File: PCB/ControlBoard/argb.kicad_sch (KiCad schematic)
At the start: 6 parts, among them J3 ARGB, U3 74AHC2G125

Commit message: First pass of PCB rework.
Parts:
- C6: footprint Capacitor_SMD:C_0805_2012Metric -> Capacitor_SMD:C_0603_1608Metric
- R3: footprint Resistor_SMD:R_0805_2012Metric -> Resistor_SMD:R_0603_1608Metric
- U3: footprint (none) -> Package_SO:TSSOP-8_3x3mm_P0.65mm
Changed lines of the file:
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@@
       (effects (font (size 1.27 1.27)) (justify left) hide)
     )
-    (property "Footprint" "" (at 33.02 22.86 0)
+    (property "Footprint" "Package_SO:TSSOP-8_3x3mm_P0.65mm" (at 33.02 22.86 0)
       (effects (font (size 1.27 1.27)) hide)
     )
@@
       (effects (font (size 1.27 1.27)))
     )
-    (property "Footprint" "" (at 68.58 24.13 0)
+    (property "Footprint" "Package_SO:TSSOP-8_3x3mm_P0.65mm" (at 68.58 24.13 0)
       (effects (font (size 1.27 1.27)) hide)
     )
@@
       (effects (font (size 1.27 1.27)))
     )
-    (property "Footprint" "" (at 68.58 39.37 0)
+    (property "Footprint" "Package_SO:TSSOP-8_3x3mm_P0.65mm" (at 68.58 39.37 0)
       (effects (font (size 1.27 1.27)) hide)
     )
@@
       (effects (font (size 1.27 1.27)) (justify left))
     )
-    (property "Footprint" "Capacitor_SMD:C_0805_2012Metric" (at 20.32 29.21 0)
+    (property "Footprint" "Capacitor_SMD:C_0603_1608Metric" (at 20.32 29.21 0)
       (effects (font (size 1.27 1.27)) hide)
     )
@@
       (effects (font (size 1.27 1.27)) (justify left))
     )
-    (property "Footprint" "Resistor_SMD:R_0805_2012Metric" (at 35.56 54.61 0)
+    (property "Footprint" "Resistor_SMD:R_0603_1608Metric" (at 35.56 54.61 0)
       (effects (font (size 1.27 1.27)) hide)
     )
@@
       (effects (font (size 1.27 1.27)) (justify left))
     )
-    (property "Footprint" "Resistor_SMD:R_0805_2012Metric" (at 35.56 62.23 0)
-      (effects (font (size 1.27 1.27)) hide)
-    )
+    (property "Footprint" "Resistor_SMD:R_0603_1608Metric" (at 35.56 62.23 0)
+      (effects (font (size 1.27 1.27)) hide)
+    )

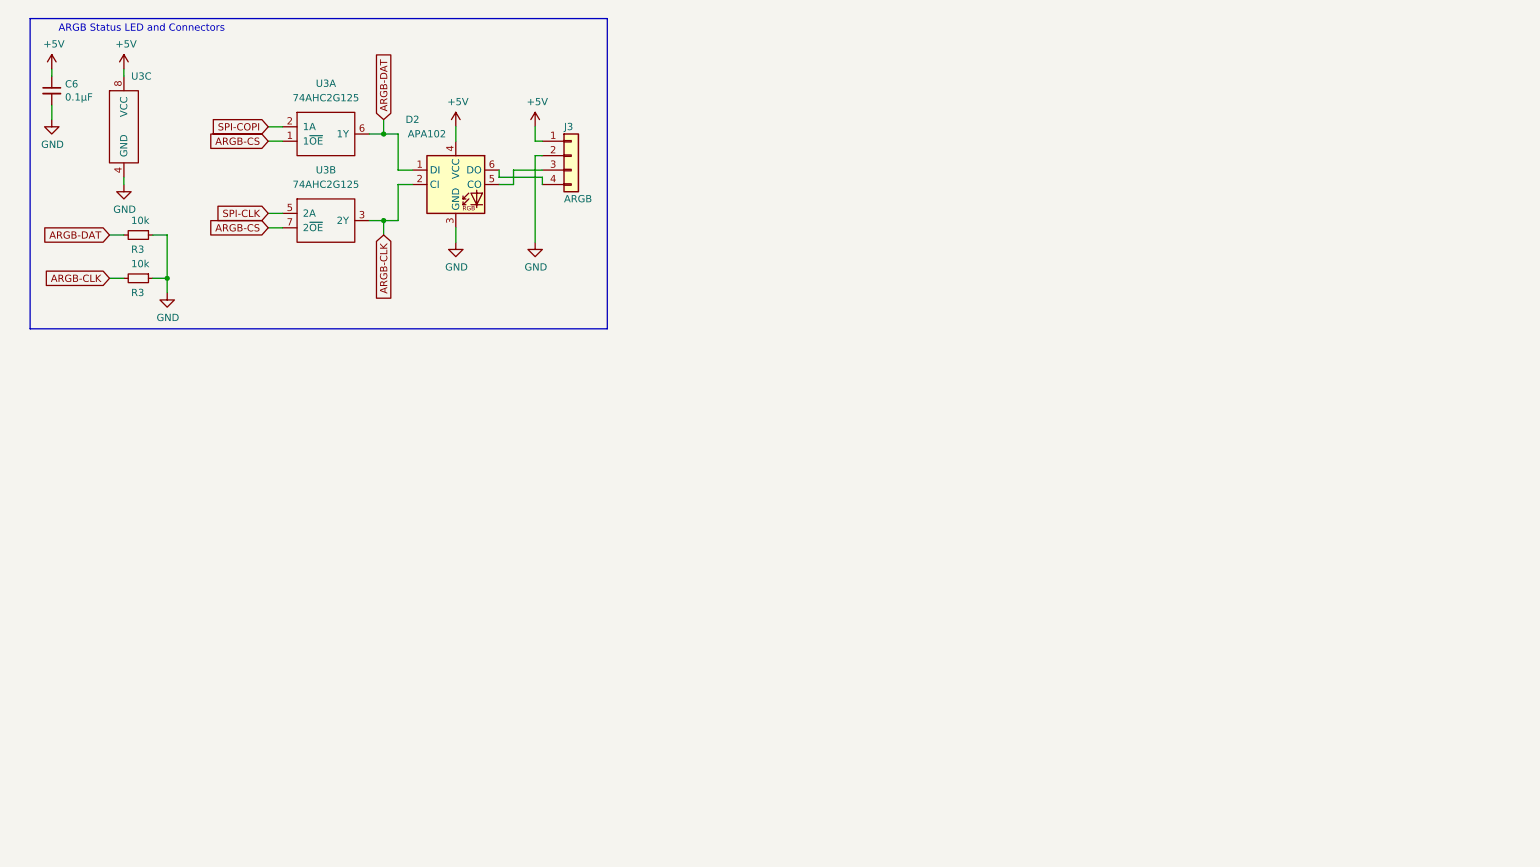
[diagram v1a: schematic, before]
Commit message: ControlBoard B02, with buck regulator fix.
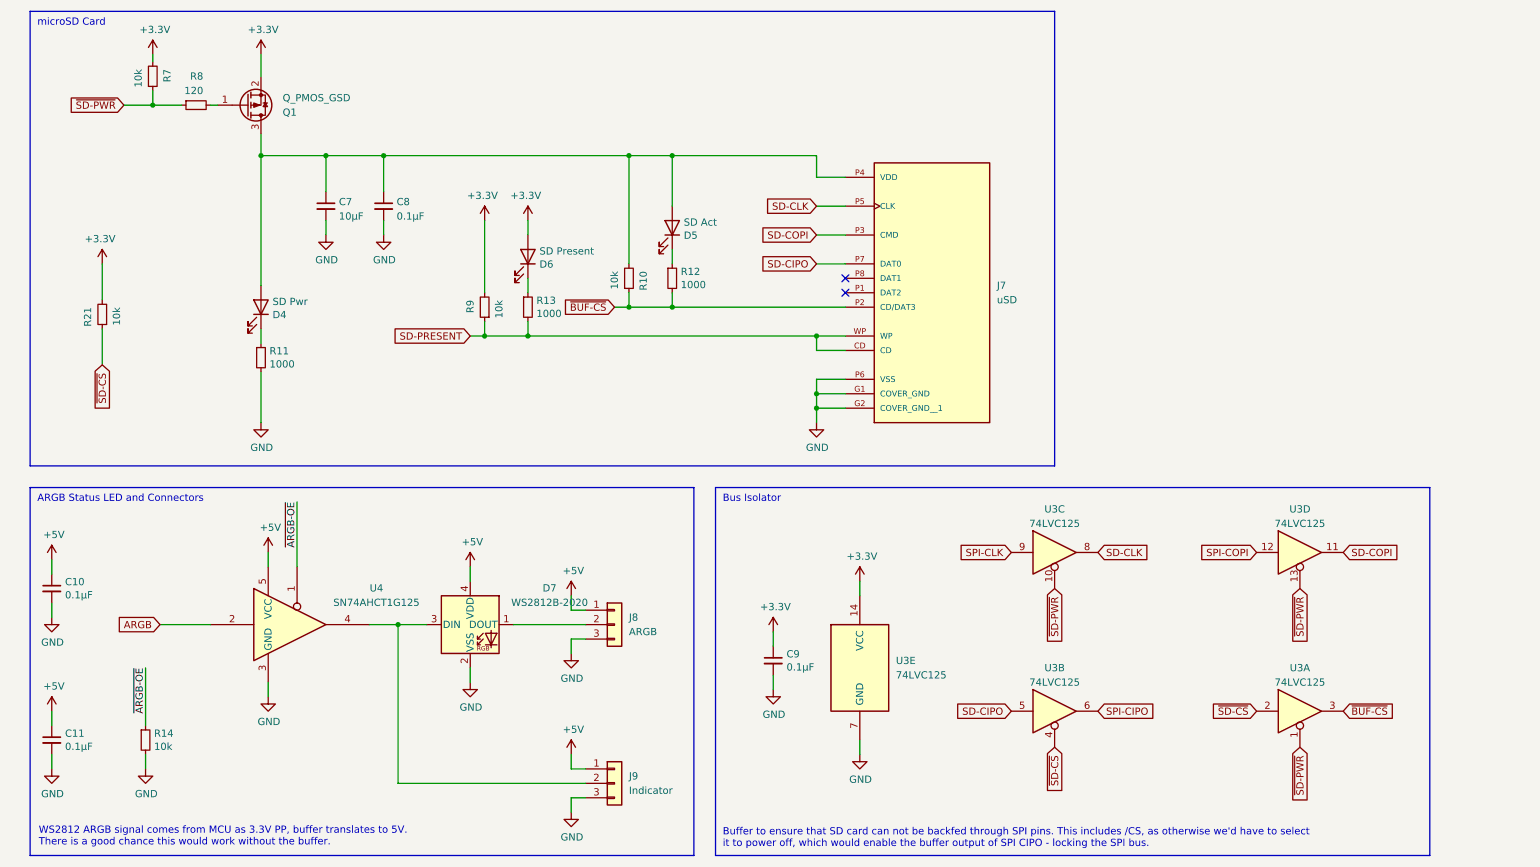
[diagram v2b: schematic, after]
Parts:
- removed C6: 0.1μF, Capacitor_SMD:C_0603_1608Metric, symbol Device:C_Small
- removed D2: APA102, LED_SMD:LED_RGB_5050-6, symbol LED:APA102
- removed J3: ARGB, Connector_JST:JST_PH_B4B-PH-SM4-TB_1x04-1MP_P2.00mm_Vertical, symbol Connector_Generic:Conn_01x04
- removed R3 (x2): 10k, Resistor_SMD:R_0603_1608Metric, symbol Device:R_Small
- removed U3: 74AHC2G125, Package_SO:TSSOP-8_3x3mm_P0.65mm, symbol KTANE:74AHC2G125
- added C10, C11, C8, C9: 0.1μF, Capacitor_SMD:C_0603_1608Metric, symbol Device:C_Small
- added C7: 10μF, Capacitor_SMD:C_0603_1608Metric, symbol Device:C_Small
- added D4: SD Pwr, LED_SMD:LED_0603_1608Metric, symbol Device:LED
- added D5: SD Act, LED_SMD:LED_0603_1608Metric, symbol Device:LED
- added D6: SD Present, LED_SMD:LED_0603_1608Metric, symbol Device:LED
- added D7: WS2812B-2020, LED_SMD:LED_WS2812B-2020_PLCC4_2.0x2.0mm, symbol LED:WS2812B-2020
- added J7: uSD, KTANE:CUI_MSD-11-A, symbol KTANE:MSD-11-A
- added J8: ARGB, Connector_JST:JST_PH_B3B-PH-SM4-TB_1x03-1MP_P2.00mm_Vertical, symbol Connector_Generic:Conn_01x03
- added J9: Indicator, Connector_JST:JST_PH_B3B-PH-SM4-TB_1x03-1MP_P2.00mm_Vertical, symbol Connector_Generic:Conn_01x03
- added Q1: Q_PMOS_GSD, Package_TO_SOT_SMD:SOT-23, symbol Transistor_FET:Q_PMOS_GSD
- added R10, R14, R21, R7, R9: 10k, Resistor_SMD:R_0603_1608Metric, symbol Device:R_Small
- added R11, R12, R13: 1000, Resistor_SMD:R_0603_1608Metric, symbol Device:R_Small
- added R8: 120, Resistor_SMD:R_0603_1608Metric, symbol Device:R_Small
- added U3: 74LVC125, Package_SO:TSSOP-14_4.4x5mm_P0.65mm, symbol 74xx:74LVC125
- added U4: SN74AHCT1G125, Package_TO_SOT_SMD:SOT-23-5, symbol 74xGxx:74AHCT1G125
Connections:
- net +5V: now also C10.1, C11.1, D7.4 (VDD), J8.1 (Pin_1), J9.1 (Pin_1), U4.5 (VCC)
- net GND: now also C10.2, C11.2, C7.2, C8.2, C9.2, D7.2 (VSS), J7.G1 (COVER_GND), J7.G2 (COVER_GND__1), J7.P6 (VSS), J8.3 (Pin_3), J9.3 (Pin_3), R11.2, R14.2, U3.7 (GND), U4.3 (GND)
- net SPI-CLK: now also U3.9
- net SPI-COPI: now also U3.12
- new net: D6.1 (K), R13.1
- new net: Q1.1 (G), R8.2
- new net: C7.1, C8.1, D4.2 (A), D5.2 (A), J7.P4 (VDD), Q1.3 (D), R10.2
- new net: D5.1 (K), R12.1
- new net: D7.1 (DOUT), J8.2 (Pin_2)
- new net: D7.3 (DIN), J9.2 (Pin_2), U4.4
- new net: D4.1 (K), R11.1
- new net +3.3V: C9.1, D6.2 (A), Q1.2 (S), R21.2, R7.2, R9.2, U3.14 (VCC)
- new net ARGB: U4.2
- new net SD-CIPO: J7.P7 (DAT0), U3.5
- new net SD-CLK: J7.P5 (CLK), U3.8
- new net SD-COPI: J7.P3 (CMD), U3.11
- new net SD-PRESENT: J7.CD, J7.WP, R13.2, R9.1
- new net SPI-CIPO: U3.6
- new net ~{ARGB-OE}: R14.1, U4.1
- new net ~{BUF-CS}: J7.P2 (CD/DAT3), R10.1, R12.2, U3.3
- new net ~{SD-CS}: R21.1, U3.2, U3.4
- new net ~{SD-PWR}: R7.1, R8.1, U3.1, U3.10, U3.13
- no-connect marks 0 -> 2
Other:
- note added: "Buffer to ensure that SD card can not be backfed through SPI pins. This includes /CS, as otherwise we'd have to select it to power off, which would enable the buffer output of SPI CIPO - locking the SPI bus."
- note added: "Bus Isolator"
- note added: "WS2812 ARGB signal comes from MCU as 3.3V PP, buffer translates to 5V. There is a good chance this would work without the buffer."
- note added: "microSD Card"

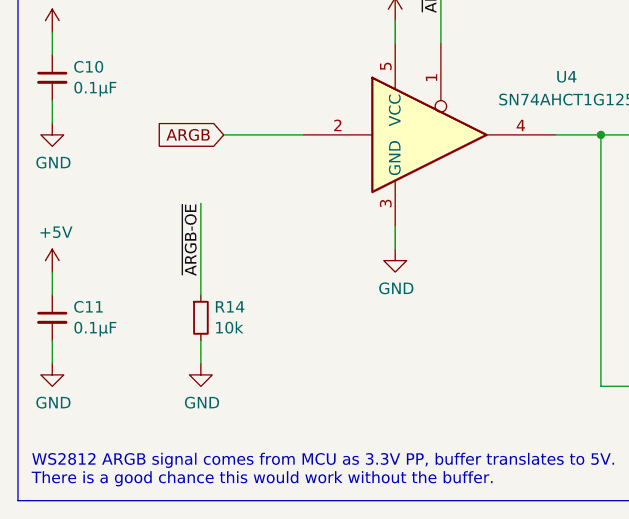
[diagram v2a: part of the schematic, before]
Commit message: Add framework for all PIC18 based firmwares.
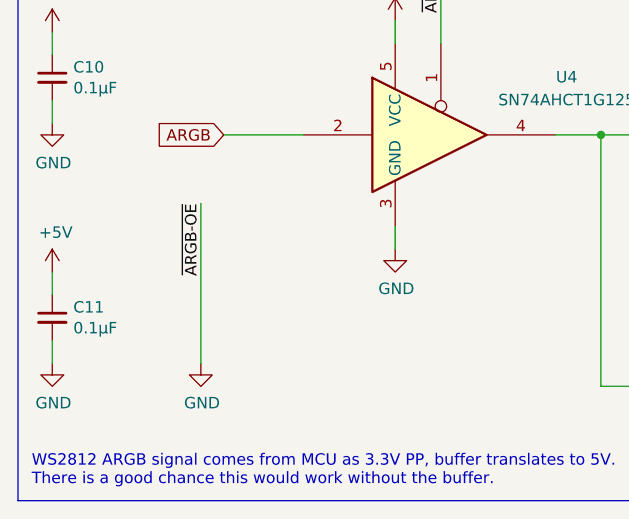
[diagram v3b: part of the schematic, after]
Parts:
- removed R14: 10k, Resistor_SMD:R_0603_1608Metric, symbol Device:R_Small
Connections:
- net ~{ARGB-OE} is gone; now on net GND: U4.1
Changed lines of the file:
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@@
 	(wire
 		(pts
-			(xy 36.83 140.97) (xy 36.83 130.81)
-		)
-		(stroke
-			(width 0)
-			(type default)
-		)
-	)
-	(wire
-		(pts
 			(xy 147.32 132.08) (xy 147.32 134.62)
 		)
@@
 	(wire
 		(pts
-			(xy 36.83 146.05) (xy 36.83 148.59)
+			(xy 36.83 130.81) (xy 36.83 148.59)
 		)
 		(stroke
@@
 					(unit 1)
 				)
-			)
-		)
-	)
-	(symbol
-		(lib_id "Device:R_Small")
-		(at 36.83 143.51 0)
-		(unit 1)
-		(exclude_from_sim no)
-		(in_bom yes)
-		(on_board yes)
-		(dnp no)
-		(property "Reference" "R14"
-			(at 38.3286 142.3416 0)
-			(effects
-				(font
-					(size 1.27 1.27)
-				)
-				(justify left)
-			)
-		)
-		(property "Value" "10k"
-			(at 38.3286 144.653 0)
-			(effects
-				(font
-					(size 1.27 1.27)
-				)
-				(justify left)
-			)
-		)
-		(property "Footprint" "Resistor_SMD:R_0603_1608Metric"
-			(at 36.83 143.51 0)
-			(effects
-				(font
-					(size 1.27 1.27)
-				)
-				(hide yes)
-			)
-		)
-		(property "Datasheet" "~"
-			(at 36.83 143.51 0)
-			(effects
-				(font
-					(size 1.27 1.27)
-				)
-				(hide yes)
-			)
-		)
-		(property "Description" "Resistor, small symbol"
-			(at 36.83 143.51 0)
-			(effects
-				(font
-					(size 1.27 1.27)
-				)
-				(hide yes)
-			)
-		)
-		(property "DIGIKEY" "P10.0KHCT-ND"
-			(at 36.83 143.51 0)
-			(effects
-				(font
-					(size 1.27 1.27)
-				)
-				(hide yes)
-			)
-		)
-		(property "Sim.Device" ""
-			(at 36.83 143.51 0)
-			(effects
-				(font
-					(size 1.27 1.27)
-				)
-				(hide yes)
-			)
-		)
-		(property "Sim.Pins" ""
-			(at 36.83 143.51 0)
-			(effects
-				(font
-					(size 1.27 1.27)
-				)
-				(hide yes)
-			)
-		)
-		(pin "1"
-		)
-		(pin "2"
-		)
-		(instances
-			(project "ControlBoard"
-				(path "/8a650ebf-3f78-4ca4-a26b-a5028693e36d/5424ff00-1761-4193-8e82-28a4c0bc55c6"
-					(reference "R14")
-					(unit 1)
-				)

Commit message: Correct Digikey part numbers.
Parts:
- Q1: DIGIKEY 4786-SSF2300CT-ND -> DMG2301L-7DICT-ND
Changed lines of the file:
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@@
 			)
 		)
-		(property "DIGIKEY" "4786-SSF2300CT-ND"
+		(property "DIGIKEY" "DMG2301L-7DICT-ND"
 			(at 54.61 31.75 0)
 			(effects
